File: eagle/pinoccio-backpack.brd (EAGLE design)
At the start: 25.4 x 43.2 mm, 2 parts

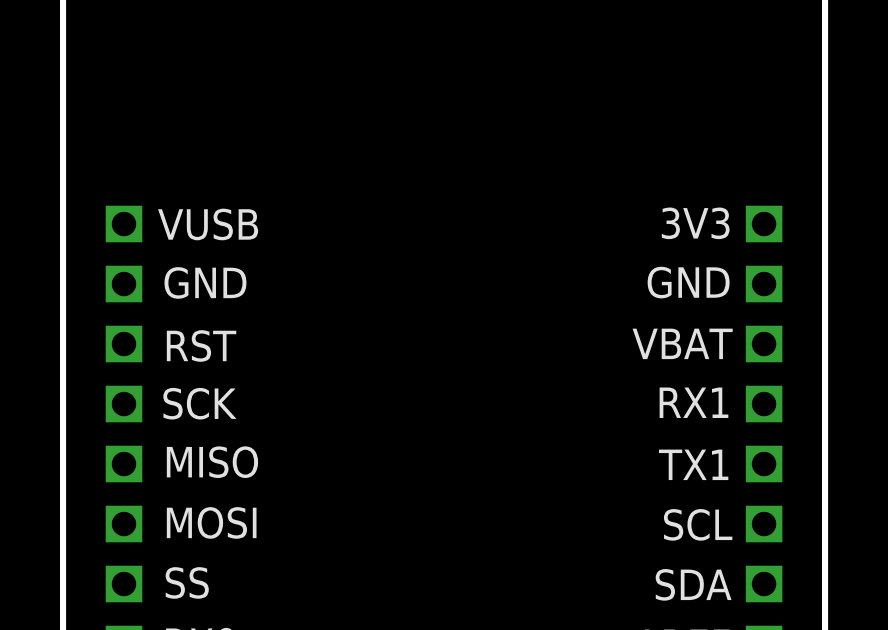
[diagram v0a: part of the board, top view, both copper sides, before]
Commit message: Updated backpack reference spec
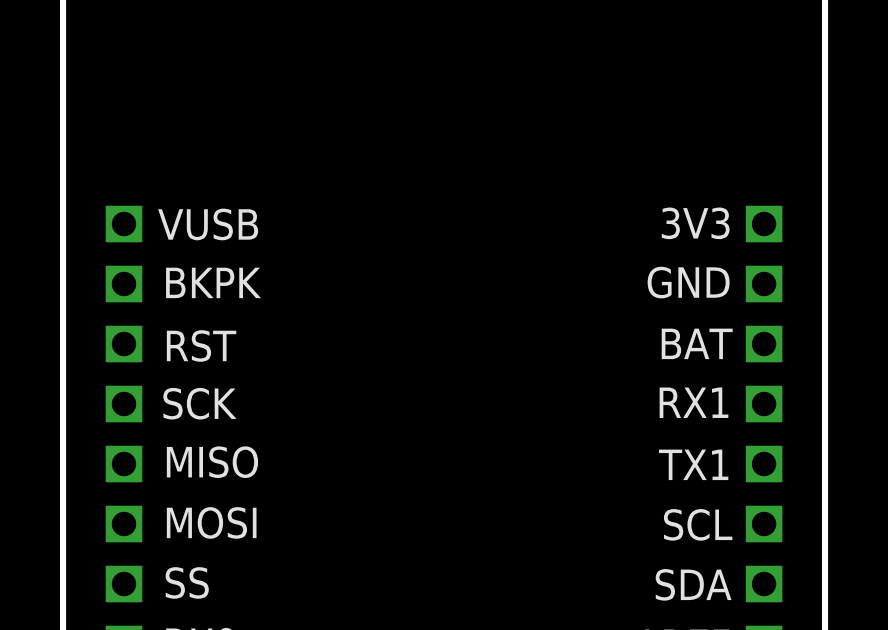
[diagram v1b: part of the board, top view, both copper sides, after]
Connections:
- net VBAT-AE renamed VBAT
- new net BKPK-BUS: JP-L.P$2
- net GND: no longer JP-L.P$2
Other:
- board text added: "BAT"
- board text added: "BKPK"
- board text added: "Pinoccio(tm) Shield Reference v0.11"
- board text removed: "Pinoccio(tm) Shield Reference v0.10"
- board text removed: "VBAT"
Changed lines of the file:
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@@
 <text x="3.3366" y="8.873" size="1.016" layer="21" font="vector" ratio="15">D8</text>
 <text x="-10.4394" y="-8.3312" size="1.27" layer="51" font="vector" ratio="15">http://pinocc.io</text>
-<text x="3.3112" y="36.8984" size="1.016" layer="21" font="vector" ratio="15">GND</text>
+<text x="3.3112" y="36.8984" size="1.016" layer="21" font="vector" ratio="15">BKPK</text>
 <text x="3.1588" y="38.8476" size="1.016" layer="21" font="vector" ratio="15">VUSB</text>
 <text x="22.3174" y="39.9016" size="1.016" layer="21" font="vector" ratio="15" rot="R180">3V3</text>
 <text x="22.292" y="37.927" size="1.016" layer="21" font="vector" ratio="15" rot="R180">GND</text>
 <text x="22.292" y="33.9204" size="1.016" layer="21" font="vector" ratio="15" rot="R180">RX1</text>
-<text x="22.3174" y="35.8828" size="1.016" layer="21" font="vector" ratio="15" rot="R180">VBAT</text>
+<text x="22.3174" y="35.8828" size="1.016" layer="21" font="vector" ratio="15" rot="R180">BAT</text>
 <text x="22.292" y="31.8508" size="1.016" layer="21" font="vector" ratio="15" rot="R180">TX1</text>
 <text x="22.3174" y="29.8508" size="1.016" layer="21" font="vector" ratio="15" rot="R180">SCL</text>
 <text x="-10.414" y="-6.604" size="1.27" layer="51" font="vector" ratio="15">Design by: Eric Jennings for Pinoccio</text>
-<text x="-10.3632" y="-4.8514" size="1.778" layer="51" font="vector" ratio="15">Pinoccio(tm) Shield Reference v0.10</text>
+<text x="-10.3632" y="-4.8514" size="1.778" layer="51" font="vector" ratio="15">Pinoccio(tm) Shield Reference v0.11</text>
 <wire x1="0" y1="50.8" x2="25.4" y2="50.8" width="0.2032" layer="20"/>
 <text x="3.3366" y="28.8984" size="1.016" layer="21" font="vector" ratio="15">MOSI</text>
@@
 <signals>
 <signal name="GND" class="5">
-<contactref element="JP-L" pad="P$2"/>
 <contactref element="JP-R" pad="P$2"/>
 <polygon width="0.4064" layer="1">
@@
 <vertex x="0.1016" y="50.8762"/>
 </polygon>
-<wire x1="2.032" y1="37.37" x2="23.368" y2="37.37" width="0" layer="19" extent="1-1"/>
 </signal>
 <signal name="MOSI">
@@
 <contactref element="JP-L" pad="P$1"/>
 </signal>
-<signal name="VBAT-AE">
-<contactref element="JP-R" pad="P$3"/>
-<wire x1="23.368" y1="35.3568" x2="23.368" y2="35.37" width="0.3048" layer="16"/>
-</signal>
 <signal name="SSN">
 <contactref element="JP-L" pad="P$7"/>
@@
 <wire x1="2.032" y1="9.3726" x2="2.032" y2="9.37" width="0.3048" layer="16"/>
 </signal>
+<signal name="BKPK-BUS">
+<contactref element="JP-L" pad="P$2"/>
+</signal>
+<signal name="VBAT">
+<contactref element="JP-R" pad="P$3"/>
+</signal>
 </signals>

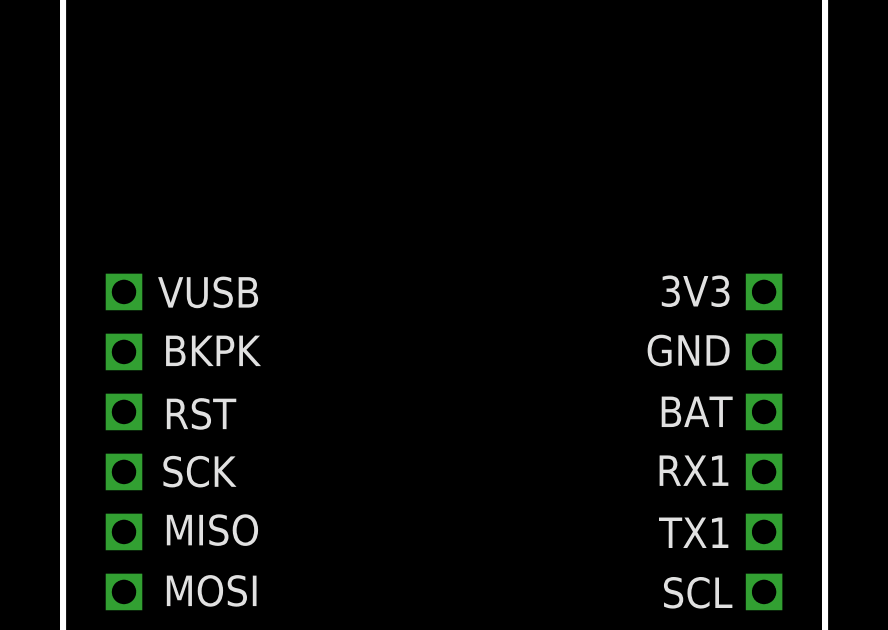
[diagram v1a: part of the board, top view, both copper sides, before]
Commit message: Add ATtiny13 support for backpack bus
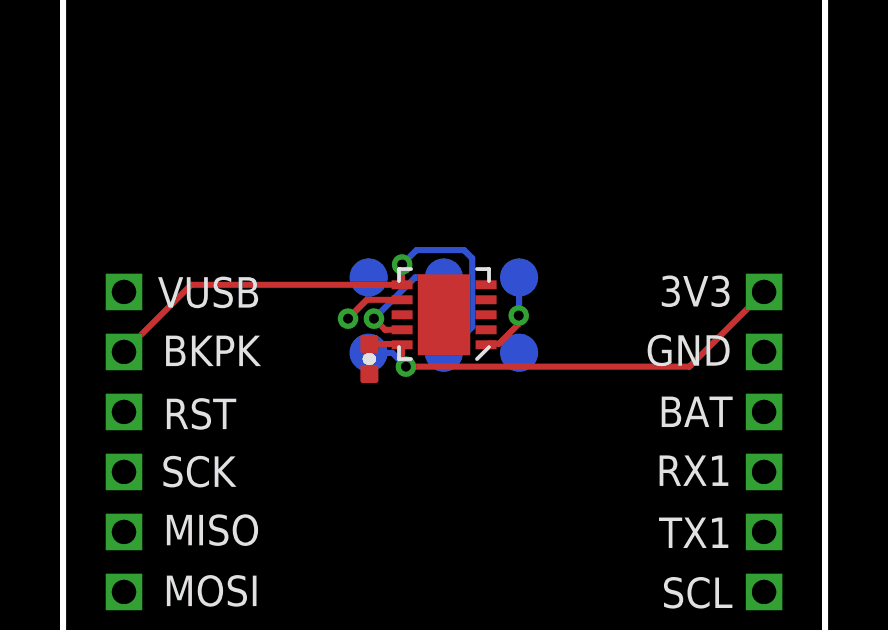
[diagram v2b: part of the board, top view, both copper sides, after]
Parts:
- added C7: 0.1uf, Pinoccio:0402-CAP
- added J1: AVR_SPI_PRG_6, Pinoccio:2X3-PAD
- added U$3: ATTINY13QFN10, Pinoccio:QFN-10
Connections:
- new net N$2: J1.1, U$3.7
- new net N$3: J1.3, U$3.9
- new net N$4: J1.5, U$3.1
- net BKPK-BUS: now also J1.4, U$3.6
- net GND: now also C7.2, J1.6, U$3.5, U$3.EP
- net VCC-AE: now also C7.1, J1.2, U$3.10
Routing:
- net BKPK-BUS: track 0.00 -> 17.1 mm, vias 0 -> 1
- net VCC-AE: track 0.00 -> 16.3 mm, vias 0 -> 1
- net N$3: track 0.00 -> 3.99 mm, vias 0 -> 1
- net N$2: track 0.00 -> 3.72 mm, vias 0 -> 1
- net N$4: track 0.00 -> 2.93 mm, vias 0 -> 1
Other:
- board text added: "Pinoccio(tm) Backpack Reference v0.11"
- board text removed: "Pinoccio(tm) Shield Reference v0.11"
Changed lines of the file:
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@@
 <setting verticaltext="up"/>
 </settings>
-<grid distance="10" unitdist="mil" unit="mil" style="lines" multiple="1" display="yes" altdistance="0.001" altunitdist="inch" altunit="inch"/>
+<grid distance="1" unitdist="mil" unit="mil" style="lines" multiple="1" display="yes" altdistance="0.001" altunitdist="inch" altunit="inch"/>
 <layers>
 <layer number="1" name="Top" color="4" fill="1" visible="yes" active="yes"/>
@@
 <text x="22.3174" y="29.8508" size="1.016" layer="21" font="vector" ratio="15" rot="R180">SCL</text>
 <text x="-10.414" y="-6.604" size="1.27" layer="51" font="vector" ratio="15">Design by: Eric Jennings for Pinoccio</text>
-<text x="-10.3632" y="-4.8514" size="1.778" layer="51" font="vector" ratio="15">Pinoccio(tm) Shield Reference v0.11</text>
+<text x="-10.3632" y="-4.8514" size="1.778" layer="51" font="vector" ratio="15">Pinoccio(tm) Backpack Reference v0.11</text>
 <wire x1="0" y1="50.8" x2="25.4" y2="50.8" width="0.2032" layer="20"/>
 <text x="3.3366" y="28.8984" size="1.016" layer="21" font="vector" ratio="15">MOSI</text>
@@
 <element name="JP-R" library="Pinoccio" package="1X16_2MM" value="M162MM" x="23.368" y="39.37" locked="yes" smashed="yes" rot="R270"/>
 <element name="JP-L" library="Pinoccio" package="1X16_2MM" value="M162MM" x="2.032" y="39.37" locked="yes" smashed="yes" rot="R270"/>
+<element name="U$3" library="Pinoccio" package="QFN-10" value="ATTINY13QFN10" x="12.7" y="38.608" rot="R180"/>
+<element name="J1" library="Pinoccio" package="2X3-PAD" value="AVR_SPI_PRG_6" x="10.1854" y="39.8526" rot="MR180"/>
+<element name="C7" library="Pinoccio" package="0402-CAP" value="0.1uf" x="10.2108" y="37.1348" smashed="yes" rot="R270"/>
 </elements>
 <signals>
@@
 <vertex x="0.1016" y="50.8762"/>
 </polygon>
+<contactref element="U$3" pad="EP"/>
+<contactref element="U$3" pad="5"/>
+<contactref element="C7" pad="2"/>
+<contactref element="J1" pad="6"/>
 </signal>
 <signal name="MOSI">
@@
 <signal name="VCC-AE">
 <contactref element="JP-R" pad="P$1"/>
+<contactref element="U$3" pad="10"/>
+<contactref element="C7" pad="1"/>
+<contactref element="J1" pad="2"/>
+<wire x1="11.3" y1="37.608" x2="11.3" y2="37.0362" width="0.2032" layer="1"/>
+<wire x1="11.3" y1="37.0362" x2="11.43" y2="36.8808" width="0.2032" layer="1"/>
+<via x="11.43" y="36.8808" extent="1-16" drill="0.3302"/>
+<wire x1="11.43" y1="36.8808" x2="10.9794" y2="37.338" width="0.2032" layer="16"/>
+<wire x1="10.9794" y1="37.338" x2="10.1854" y2="37.3446" width="0.2032" layer="16"/>
+<wire x1="11.3" y1="37.608" x2="11.276" y2="37.584" width="0.2032" layer="1"/>
+<wire x1="11.276" y1="37.584" x2="11.2252" y2="37.6348" width="0.2032" layer="1"/>
+<wire x1="11.2252" y1="37.6348" x2="10.2108" y2="37.6348" width="0.2032" layer="1"/>
+<wire x1="23.368" y1="39.37" x2="20.8788" y2="36.8808" width="0.2032" layer="1"/>
+<wire x1="20.8788" y1="36.8808" x2="11.43" y2="36.8808" width="0.2032" layer="1"/>
 </signal>
 <signal name="VIN">
@@
 <signal name="BKPK-BUS">
 <contactref element="JP-L" pad="P$2"/>
+<contactref element="J1" pad="4"/>
+<contactref element="U$3" pad="6"/>
+<wire x1="11.3" y1="39.608" x2="11.303" y2="39.611" width="0.2032" layer="1"/>
+<via x="11.303" y="40.2844" extent="1-16" drill="0.3302"/>
+<wire x1="11.303" y1="40.2844" x2="11.7856" y2="40.767" width="0.2032" layer="16"/>
+<wire x1="11.7856" y1="40.767" x2="13.3604" y2="40.767" width="0.2032" layer="16"/>
+<wire x1="13.3604" y1="40.767" x2="13.6398" y2="40.4876" width="0.2032" layer="16"/>
+<wire x1="13.6398" y1="40.4876" x2="13.6398" y2="38.2016" width="0.2032" layer="16"/>
+<wire x1="13.6398" y1="38.2016" x2="12.7828" y2="37.3446" width="0.2032" layer="16"/>
+<wire x1="12.7828" y1="37.3446" x2="12.6934" y2="37.3446" width="0.2032" layer="16"/>
+<wire x1="11.303" y1="40.2844" x2="11.3" y2="40.2814" width="0.2032" layer="1"/>
+<wire x1="11.3" y1="40.2814" x2="11.3" y2="39.608" width="0.2032" layer="1"/>
+<wire x1="2.032" y1="37.37" x2="4.27" y2="39.608" width="0.2032" layer="1"/>
+<wire x1="4.27" y1="39.608" x2="11.3" y2="39.608" width="0.2032" layer="1"/>
 </signal>
 <signal name="VBAT">
 <contactref element="JP-R" pad="P$3"/>
 </signal>
+<signal name="N$2">
+<contactref element="J1" pad="1"/>
+<contactref element="U$3" pad="7"/>
+<wire x1="11.3" y1="39.108" x2="10.1266" y2="39.108" width="0.2032" layer="1"/>
+<wire x1="10.1266" y1="39.108" x2="9.4996" y2="38.481" width="0.2032" layer="1"/>
+<via x="9.4996" y="38.481" extent="1-16" drill="0.3302"/>
+<wire x1="9.4996" y1="38.481" x2="10.1854" y2="39.1668" width="0.2032" layer="16"/>
+<wire x1="10.1854" y1="39.1668" x2="10.1854" y2="39.8526" width="0.2032" layer="16"/>
+</signal>
+<signal name="N$3">
+<contactref element="J1" pad="3"/>
+<contactref element="U$3" pad="9"/>
+<wire x1="11.3" y1="38.108" x2="10.7362" y2="38.108" width="0.2032" layer="1"/>
+<wire x1="10.7362" y1="38.108" x2="10.3632" y2="38.481" width="0.2032" layer="1"/>
+<via x="10.3632" y="38.481" extent="1-16" drill="0.3302"/>
+<wire x1="10.3632" y1="38.481" x2="11.7348" y2="39.8526" width="0.2032" layer="16"/>
+<wire x1="11.7348" y1="39.8526" x2="12.6934" y2="39.8526" width="0.2032" layer="16"/>
+</signal>
+<signal name="N$4">
+<contactref element="J1" pad="5"/>
+<contactref element="U$3" pad="1"/>
+<wire x1="14.1" y1="37.608" x2="14.1348" y2="37.6428" width="0.2032" layer="1"/>
+<wire x1="14.1348" y1="37.6428" x2="14.5288" y2="37.6428" width="0.2032" layer="1"/>
+<wire x1="14.5288" y1="37.6428" x2="15.1892" y2="38.3032" width="0.2032" layer="1"/>
+<wire x1="15.1892" y1="38.3032" x2="15.1892" y2="38.5826" width="0.2032" layer="1"/>
+<via x="15.1892" y="38.5826" extent="1-16" drill="0.3302"/>
+<wire x1="15.1892" y1="38.5826" x2="15.2014" y2="38.5948" width="0.2032" layer="16"/>
+<wire x1="15.2014" y1="38.5948" x2="15.2014" y2="39.8526" width="0.2032" layer="16"/>
+</signal>
 </signals>
